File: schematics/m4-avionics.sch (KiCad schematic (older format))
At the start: 21 parts, among them J1 USB, J2 USB, J4 CAMERA

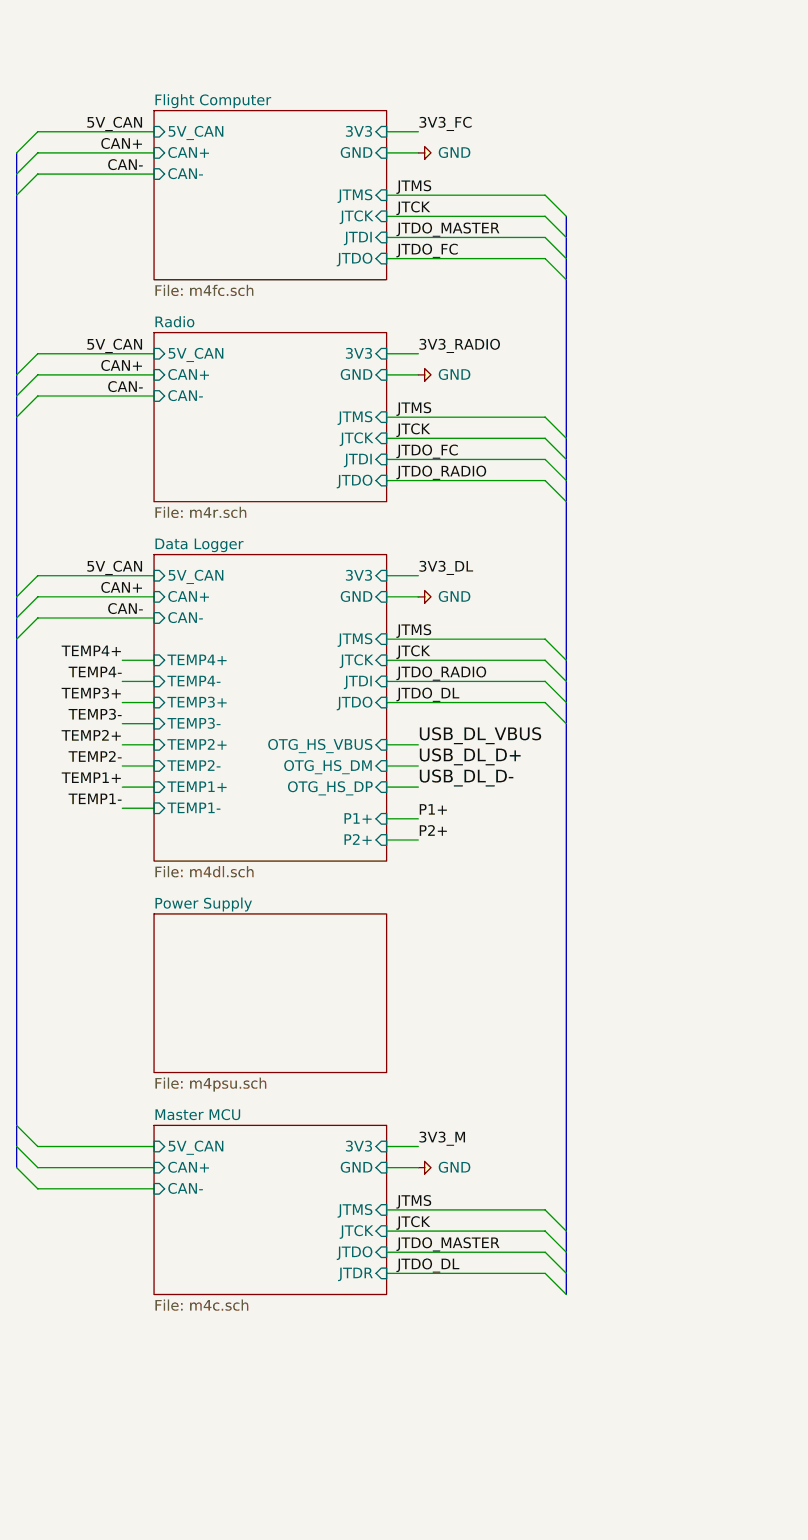
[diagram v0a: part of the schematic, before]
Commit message: Restructure main schematic bus layout
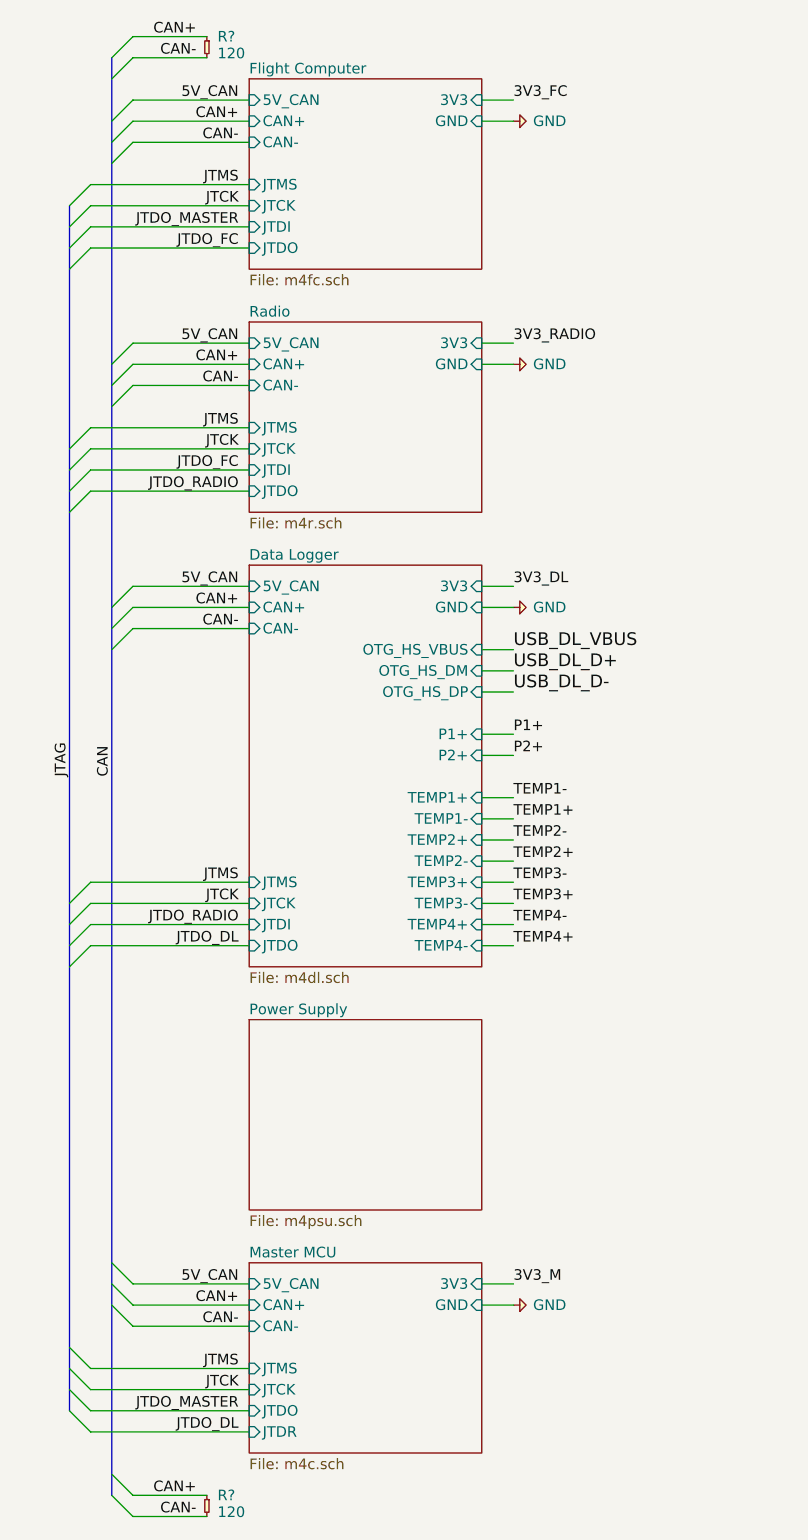
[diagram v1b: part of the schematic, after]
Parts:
- added R? (x2): 120, symbol cusf-kicad:R
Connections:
- net CAN+: now also R?.1, R?.1
- net CAN-: now also R?.2, R?.2

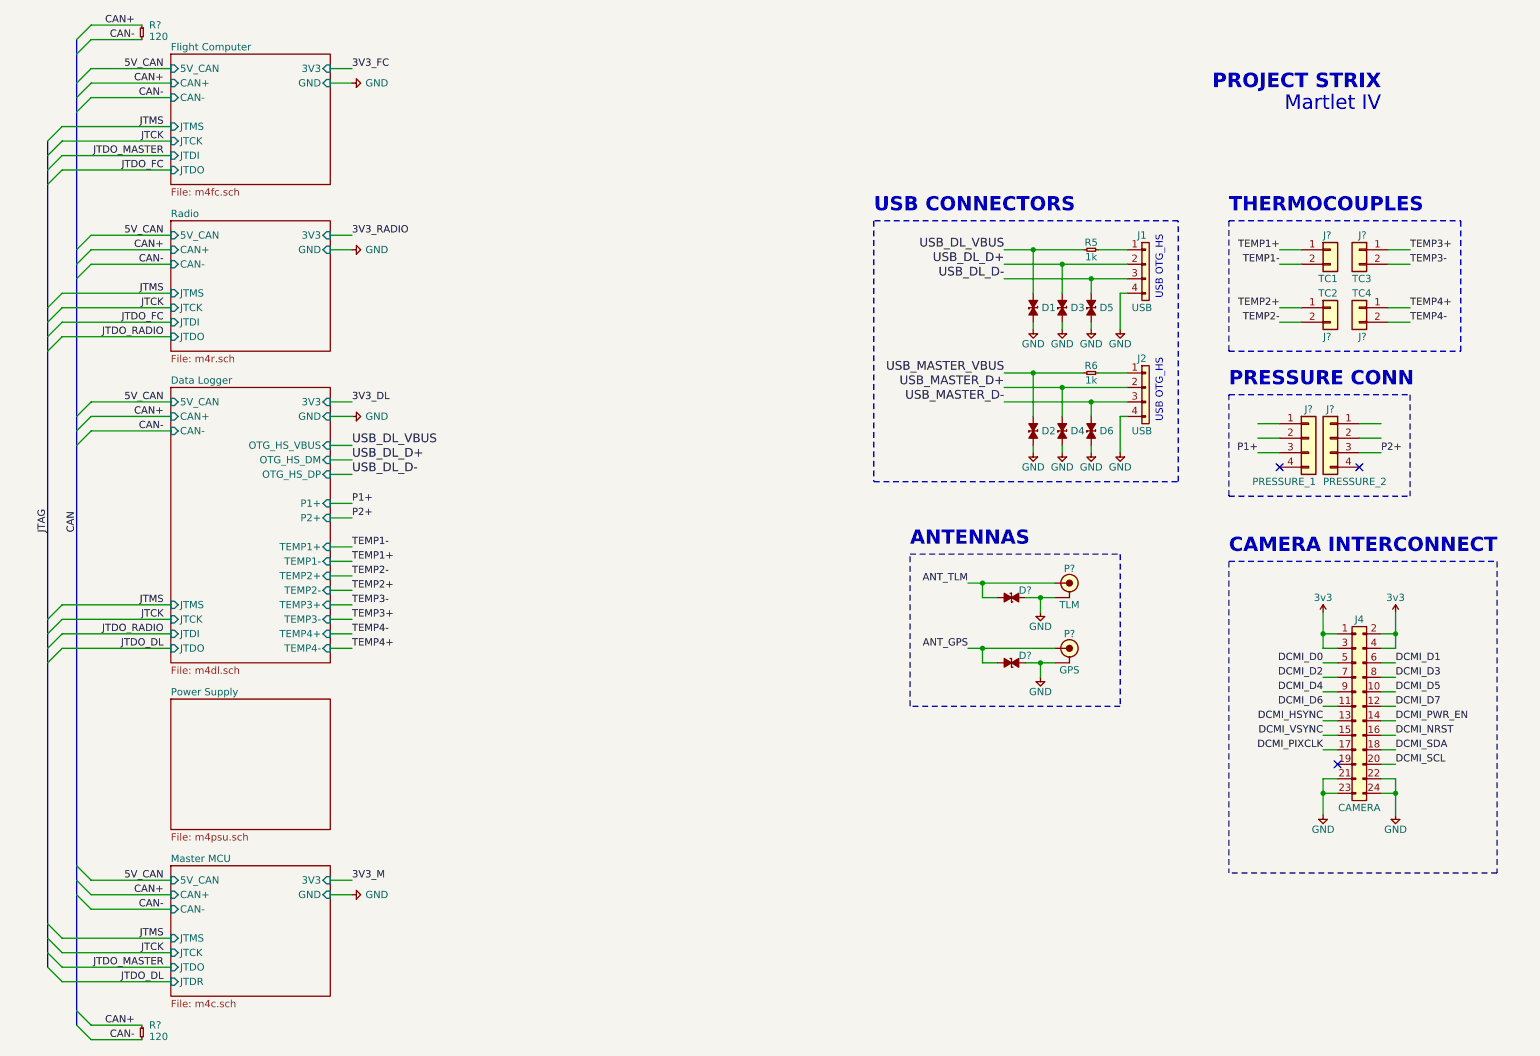
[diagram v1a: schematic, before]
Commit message: Normalise all font sizes to 50 mil
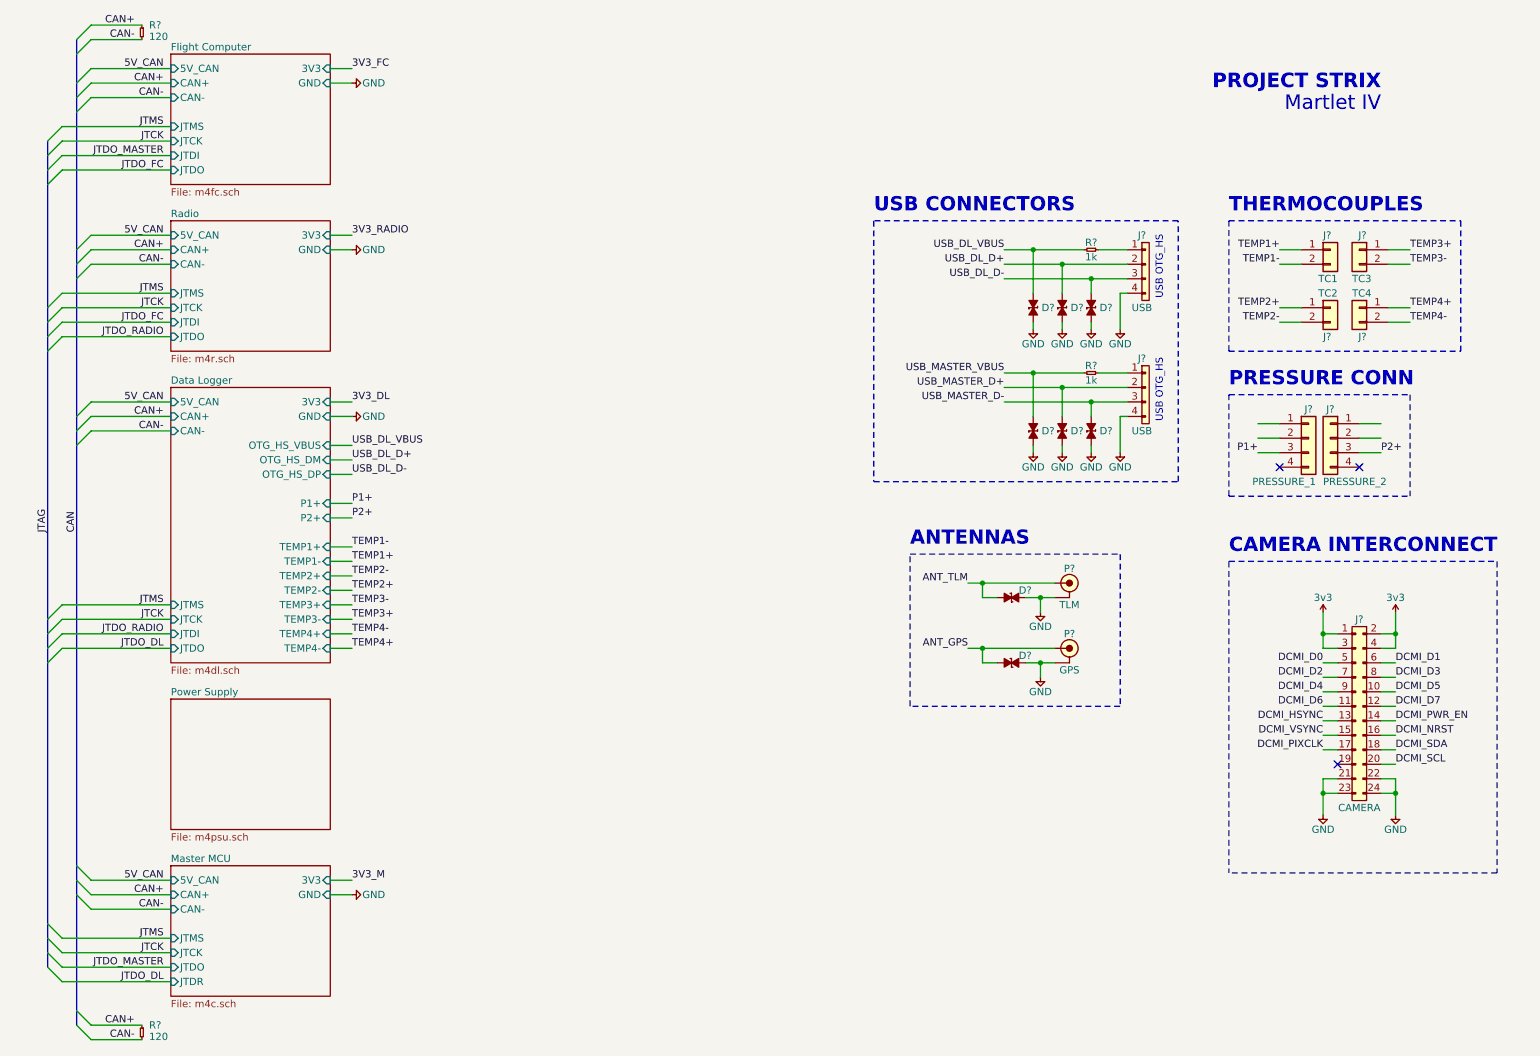
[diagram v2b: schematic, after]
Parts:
- renumbered D1 to D?, D3 to D?, D5 to D?, D2 to D?, D4 to D?, D6 to D?, J2 to J?, J1 to J?, J4 to J?, R6 to R?, R5 to R?

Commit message: Upscale logo resolution and use cusf-kicad for connector symbols
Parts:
- J? (x2): symbol Connector_Generic:Conn_01x04 -> cusf-kicad:CONN_01x04
- J? (x4): symbol Connector_Generic:Conn_01x02 -> cusf-kicad:CONN_01x02
